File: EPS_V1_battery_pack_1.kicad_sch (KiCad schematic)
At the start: 29 parts, among them U1 MP2672AGD-0000-Z, U5 MAX17205G+

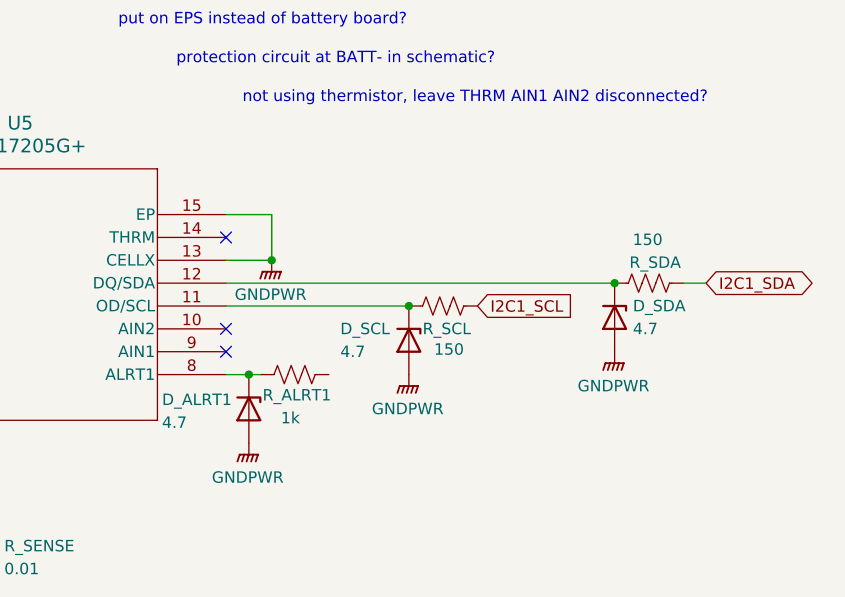
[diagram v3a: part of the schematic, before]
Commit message: Add fuel gauge ALRT lines
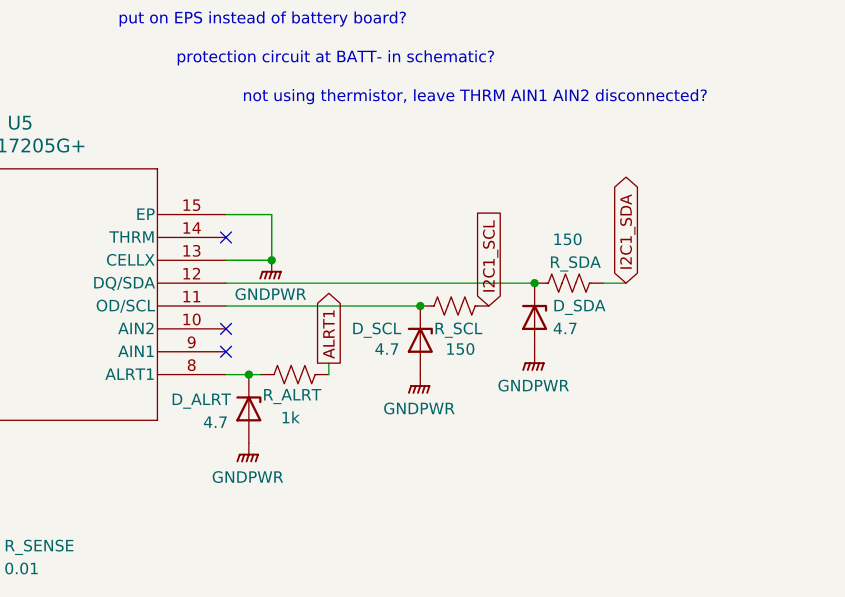
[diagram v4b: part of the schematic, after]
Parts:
- renumbered D_ALRT1 to D_ALRT, R_ALRT1 to R_ALRT
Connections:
- net ALRT1: now reaches R_ALRT.2
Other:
- moved on the sheet: D_SCL, D_SDA, R_SCL, R_SDA
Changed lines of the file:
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@@
 	)
 	(junction
-		(at 260.35 80.01)
+		(at 251.46 80.01)
 		(diameter 0)
 		(color 0 0 0 0)
@@
 	)
 	(junction
-		(at 237.49 82.55)
+		(at 238.76 82.55)
 		(diameter 0)
 		(color 0 0 0 0)
@@
 	(wire
 		(pts
+			(xy 228.6 88.9) (xy 228.6 90.17)
+		)
+		(stroke
+			(width 0)
+			(type default)
+		)
+	)
+	(wire
+		(pts
 			(xy 166.37 77.47) (xy 171.45 77.47)
 		)
@@
 	(wire
 		(pts
-			(xy 217.17 80.01) (xy 260.35 80.01)
+			(xy 217.17 80.01) (xy 251.46 80.01)
 		)
 		(stroke
@@
 	(wire
 		(pts
-			(xy 217.17 82.55) (xy 237.49 82.55)
+			(xy 217.17 82.55) (xy 238.76 82.55)
 		)
 		(stroke
@@
 	(wire
 		(pts
-			(xy 270.51 80.01) (xy 267.97 80.01)
+			(xy 261.62 80.01) (xy 259.08 80.01)
 		)
 		(stroke
@@
 		)
 	)
+	(global_label "ALRT1"
+		(shape output)
+		(at 228.6 88.9 90)
+		(fields_autoplaced yes)
+		(effects
+			(font
+				(size 1.27 1.27)
+			)
+			(justify left)
+		)
+		(property "Intersheetrefs" "${INTERSHEET_REFS}"
+			(at 228.6 80.351 90)
+			(effects
+				(font
+					(size 1.27 1.27)
+				)
+				(justify left)
+				(hide yes)
+			)
+		)
+	)
 	(global_label "I2C1_SDA"
 		(shape bidirectional)
-		(at 270.51 80.01 0)
+		(at 261.62 80.01 90)
 		(fields_autoplaced yes)
 		(effects
@@
 		)
 		(property "Intersheetrefs" "${INTERSHEET_REFS}"
-			(at 283.436 80.01 0)
+			(at 261.62 67.084 90)
 			(effects
 				(font
@@
 	(global_label "I2C1_SCL"
 		(shape input)
-		(at 245.11 82.55 0)
+		(at 246.38 82.55 90)
 		(fields_autoplaced yes)
 		(effects
@@
 		)
 		(property "Intersheetrefs" "${INTERSHEET_REFS}"
-			(at 256.8642 82.55 0)
+			(at 246.38 70.7958 90)
 			(effects
 				(font
@@
 	(symbol
 		(lib_id "Device:R_US")
-		(at 264.16 80.01 90)
+		(at 255.27 80.01 90)
 		(unit 1)
 		(exclude_from_sim no)
@@
 		(dnp no)
 		(property "Reference" "R_SDA"
-			(at 267.716 77.724 90)
+			(at 258.826 77.724 90)
 			(effects
 				(font
@@
 		)
 		(property "Value" "150"
-			(at 265.684 75.184 90)
+			(at 256.794 75.184 90)
 			(effects
 				(font
@@
 		)
 		(property "Footprint" ""
-			(at 264.414 78.994 90)
+			(at 255.524 78.994 90)
 			(effects
 				(font
@@
 		)
 		(property "Datasheet" "~"
-			(at 264.16 80.01 0)
+			(at 255.27 80.01 0)
 			(effects
 				(font
@@
 		)
 		(property "Description" "Resistor, US symbol"
-			(at 264.16 80.01 0)
+			(at 255.27 80.01 0)
 			(effects
 				(font
@@
 		(on_board yes)
 		(dnp no)
-		(property "Reference" "R_ALRT1"
+		(property "Reference" "R_ALRT"
 			(at 221.234 92.456 90)
 			(effects
@@
 			(project "EPS_V1"
 				(path "/85157432-5d03-48fa-ab40-27ed3d133f47/d6a7ca1d-fe68-467f-8233-74a5cf811189"
-					(reference "R_ALRT1")
+					(reference "R_ALRT")
 					(unit 1)
 				)
@@
 	(symbol
 		(lib_id "power:GNDPWR")
-		(at 237.49 90.17 0)
+		(at 238.76 90.17 0)
 		(unit 1)
 		(exclude_from_sim no)
@@
 		(fields_autoplaced yes)
 		(property "Reference" "#PWR043"
-			(at 237.49 95.25 0)
+			(at 238.76 95.25 0)
 			(effects
 				(font
@@
 		)
 		(property "Value" "GNDPWR"
-			(at 237.363 93.98 0)
+			(at 238.633 93.98 0)
 			(effects
 				(font
@@
 		)
 		(property "Footprint" ""
-			(at 237.49 91.44 0)
+			(at 238.76 91.44 0)
 			(effects
 				(font
@@
 		)
 		(property "Datasheet" ""
-			(at 237.49 91.44 0)
+			(at 238.76 91.44 0)
 			(effects
 				(font
@@
 		)
 		(property "Description" "Power symbol creates a global label with name \"GNDPWR\" , global ground"
-			(at 237.49 90.17 0)
+			(at 238.76 90.17 0)
 			(effects
 				(font
@@
 	(symbol
 		(lib_id "Device:D_Zener")
-		(at 260.35 83.82 270)
+		(at 251.46 83.82 270)
 		(unit 1)
 		(exclude_from_sim no)
@@
 		(dnp no)
 		(property "Reference" "D_SDA"
-			(at 262.382 82.55 90)
+			(at 253.492 82.55 90)
 			(effects
 				(font
@@
 		)
 		(property "Value" "4.7"
-			(at 262.382 85.09 90)
+			(at 253.492 85.09 90)
 			(effects
 				(font
@@
 		)
 		(property "Footprint" ""
-			(at 260.35 83.82 0)
+			(at 251.46 83.82 0)
 			(effects
 				(font
@@
 		)
 		(property "Datasheet" "~"
-			(at 260.35 83.82 0)
+			(at 251.46 83.82 0)
 			(effects
 				(font
@@
 		)
 		(property "Description" "Zener diode"
-			(at 260.35 83.82 0)
+			(at 251.46 83.82 0)
 			(effects
 				(font
@@
 	(symbol
 		(lib_id "Device:R_US")
-		(at 241.3 82.55 90)
+		(at 242.57 82.55 90)
 		(unit 1)
 		(exclude_from_sim no)
@@
 		(dnp no)
 		(property "Reference" "R_SCL"
-			(at 239.014 85.09 90)
+			(at 240.284 85.09 90)
 			(effects
 				(font
@@
 		)
 		(property "Value" "150"
-			(at 240.284 87.376 90)
+			(at 241.554 87.376 90)
 			(effects
 				(font
@@
 		)
 		(property "Footprint" ""
-			(at 241.554 81.534 90)
+			(at 242.824 81.534 90)
 			(effects
 				(font
@@
 		)
 		(property "Datasheet" "~"
-			(at 241.3 82.55 0)
+			(at 242.57 82.55 0)
 			(effects
 				(font
@@
 		)
 		(property "Description" "Resistor, US symbol"
-			(at 241.3 82.55 0)
+			(at 242.57 82.55 0)
 			(effects
 				(font
@@
 	(symbol
 		(lib_id "power:GNDPWR")
-		(at 260.35 87.63 0)
+		(at 251.46 87.63 0)
 		(unit 1)
 		(exclude_from_sim no)
@@
 		(fields_autoplaced yes)
 		(property "Reference" "#PWR044"
-			(at 260.35 92.71 0)
+			(at 251.46 92.71 0)
 			(effects
 				(font
@@
 		)
 		(property "Value" "GNDPWR"
-			(at 260.223 91.44 0)
+			(at 251.333 91.44 0)
 			(effects
 				(font
@@
 		)
 		(property "Footprint" ""
-			(at 260.35 88.9 0)
+			(at 251.46 88.9 0)
 			(effects
 				(font
@@
 		)
 		(property "Datasheet" ""
-			(at 260.35 88.9 0)
+			(at 251.46 88.9 0)
 			(effects
 				(font
@@
 		)
 		(property "Description" "Power symbol creates a global label with name \"GNDPWR\" , global ground"
-			(at 260.35 87.63 0)
+			(at 251.46 87.63 0)
 			(effects
 				(font
@@
 		(on_board yes)
 		(dnp no)
-		(property "Reference" "D_ALRT1"
-			(at 210.058 92.964 90)
+		(property "Reference" "D_ALRT"
+			(at 211.074 92.964 90)
 			(effects
 				(font
@@
 		)
 		(property "Value" "4.7"
-			(at 210.058 95.504 90)
+			(at 214.63 95.504 90)
 			(effects
 				(font
@@
 			(project ""
 				(path "/85157432-5d03-48fa-ab40-27ed3d133f47/d6a7ca1d-fe68-467f-8233-74a5cf811189"
-					(reference "D_ALRT1")
+					(reference "D_ALRT")
 					(unit 1)
 				)
@@
 	(symbol
 		(lib_id "Device:D_Zener")
-		(at 237.49 86.36 270)
+		(at 238.76 86.36 270)
 		(unit 1)
 		(exclude_from_sim no)
@@
 		(dnp no)
 		(property "Reference" "D_SCL"
-			(at 229.87 85.09 90)
+			(at 231.14 85.09 90)
 			(effects
 				(font
@@
 		)
 		(property "Value" "4.7"
-			(at 229.87 87.63 90)
+			(at 233.68 87.376 90)
 			(effects
 				(font
@@
 		)
 		(property "Footprint" ""
-			(at 237.49 86.36 0)
+			(at 238.76 86.36 0)
 			(effects
 				(font
@@
 		)
 		(property "Datasheet" "~"
-			(at 237.49 86.36 0)
+			(at 238.76 86.36 0)
 			(effects
 				(font
@@
 		)
 		(property "Description" "Zener diode"
-			(at 237.49 86.36 0)
+			(at 238.76 86.36 0)
 			(effects
 				(font

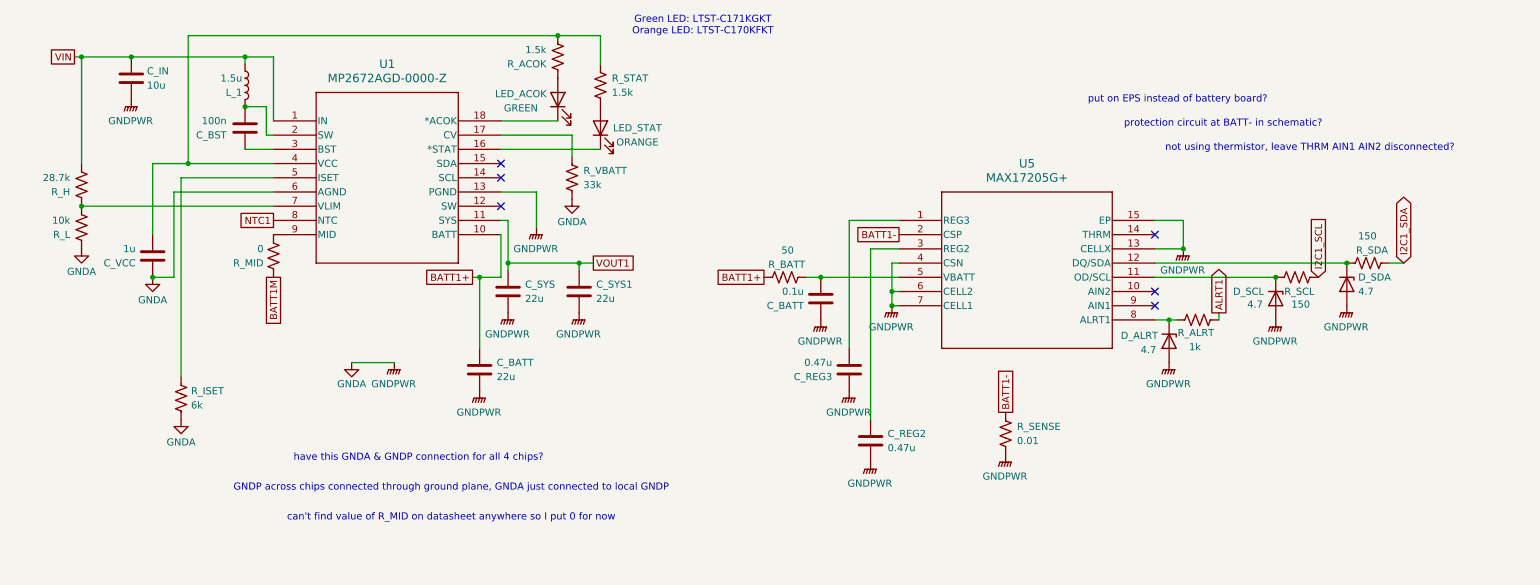
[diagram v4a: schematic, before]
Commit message: Add boost converter to 12V, fix grounding
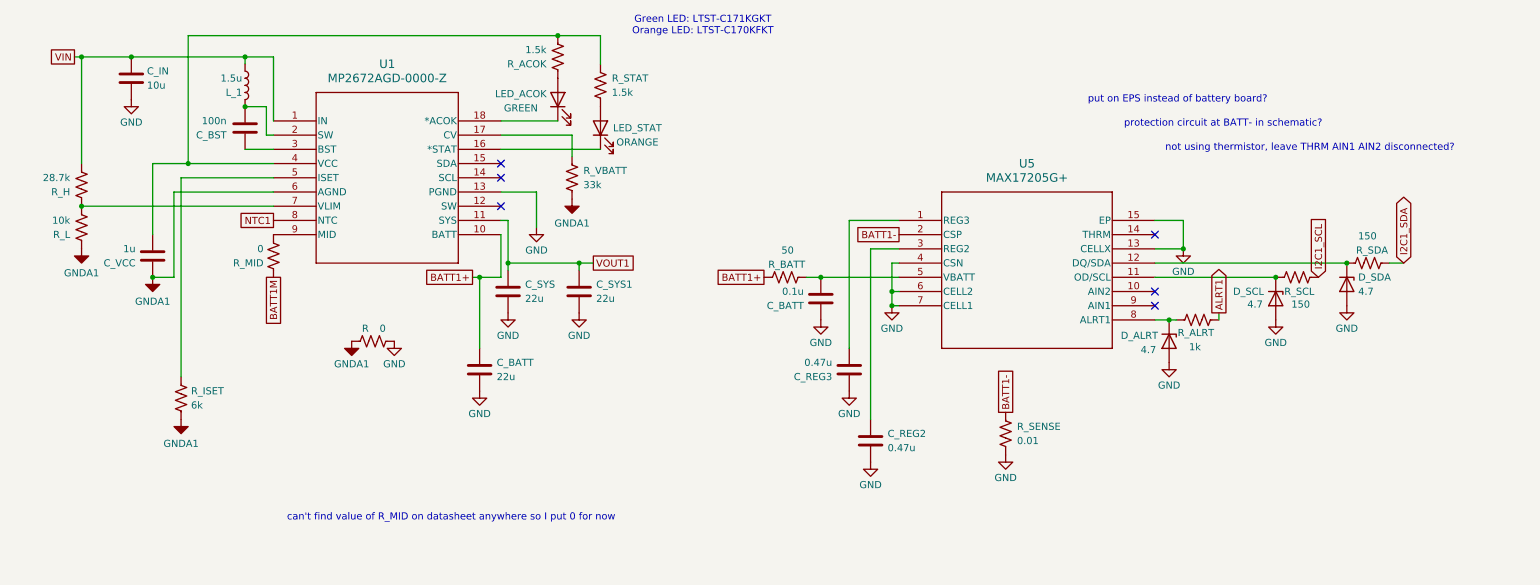
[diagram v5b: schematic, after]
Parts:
- added R: 0, symbol Device:R_US
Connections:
- net GNDA renamed GND
- net GND: now also R.2; no longer C_VCC.1, R_ISET.2, R_L.1, R_VBATT.2, U1.6 (AGND)
- new net GNDA1: C_VCC.1, R.1, R_ISET.2, R_L.1, R_VBATT.2, U1.6 (AGND)
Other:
- note removed: "GNDP across chips connected through ground plane, GNDA just connected to local GNDP"
- note removed: "have this GNDA & GNDP connection for all 4 chips?"

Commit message: Add 12V boost values
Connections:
- net GND: no longer R_SENSE.2
- new net BATT_GND: R_SENSE.2
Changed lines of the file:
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@@
+		)
+	)
+	(global_label "BATT_GND"
+		(shape passive)
+		(at 190.5 114.3 270)
+		(fields_autoplaced yes)
+		(effects
+			(font
+				(size 1.27 1.27)
+			)
+			(justify right)
+		)
+		(property "Intersheetrefs" "${INTERSHEET_REFS}"
+			(at 190.5 125.3058 90)
+			(effects
+				(font
+					(size 1.27 1.27)
+				)
+				(justify right)
+				(hide yes)
+			)
 		)
 	)
@@
 					(unit 1)
 				)
-			)
-		)
-	)
-	(symbol
-		(lib_id "power:GND")
-		(at 190.5 114.3 0)
-		(unit 1)
-		(exclude_from_sim no)
-		(in_bom yes)
-		(on_board yes)
-		(dnp no)
-		(property "Reference" "#PWR03"
-			(at 190.5 120.65 0)
-			(effects
-				(font
-					(size 1.27 1.27)
-				)
-				(hide yes)
-			)
-		)
-		(property "Value" "GND"
-			(at 190.5 118.364 0)
-			(effects
-				(font
-					(size 1.27 1.27)
-				)
-			)
-		)
-		(property "Footprint" ""
-			(at 190.5 114.3 0)
-			(effects
-				(font
-					(size 1.27 1.27)
-				)
-				(hide yes)
-			)
-		)
-		(property "Datasheet" ""
-			(at 190.5 114.3 0)
-			(effects
-				(font
-					(size 1.27 1.27)
-				)
-				(hide yes)
-			)
-		)
-		(property "Description" "Power symbol creates a global label with name \"GND\" , ground"
-			(at 190.5 114.3 0)
-			(effects
-				(font
-					(size 1.27 1.27)
-				)
-				(hide yes)
-			)
-		)
-		(pin "1"
-		)
-		(instances
-			(project "EPS_V1"
-				(path "/85157432-5d03-48fa-ab40-27ed3d133f47/d6a7ca1d-fe68-467f-8233-74a5cf811189"
-					(reference "#PWR03")
-					(unit 1)
-				)

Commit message: Clarify global net naming, other minor fixes
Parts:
- added R7: 0, symbol Device:R_US
- R_MID: value 0 -> 50
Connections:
- net BATT_GND: now also R7.1; no longer R_SENSE.2
- net GND: no longer U5.15 (EP), U5.4 (CSN)
- net VIN renamed CHG_IN
- net VOUT1 renamed CHG_OUT1
- new net: R7.2, R_SENSE.2, U5.15 (EP), U5.4 (CSN)
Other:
- note added: "50 ohm R_MID value from fuel gauge datasheet"
- note removed: "protection circuit at BATT- in schematic?"
- note removed: "put on EPS instead of battery board?"
- moved on the sheet: R_SENSE

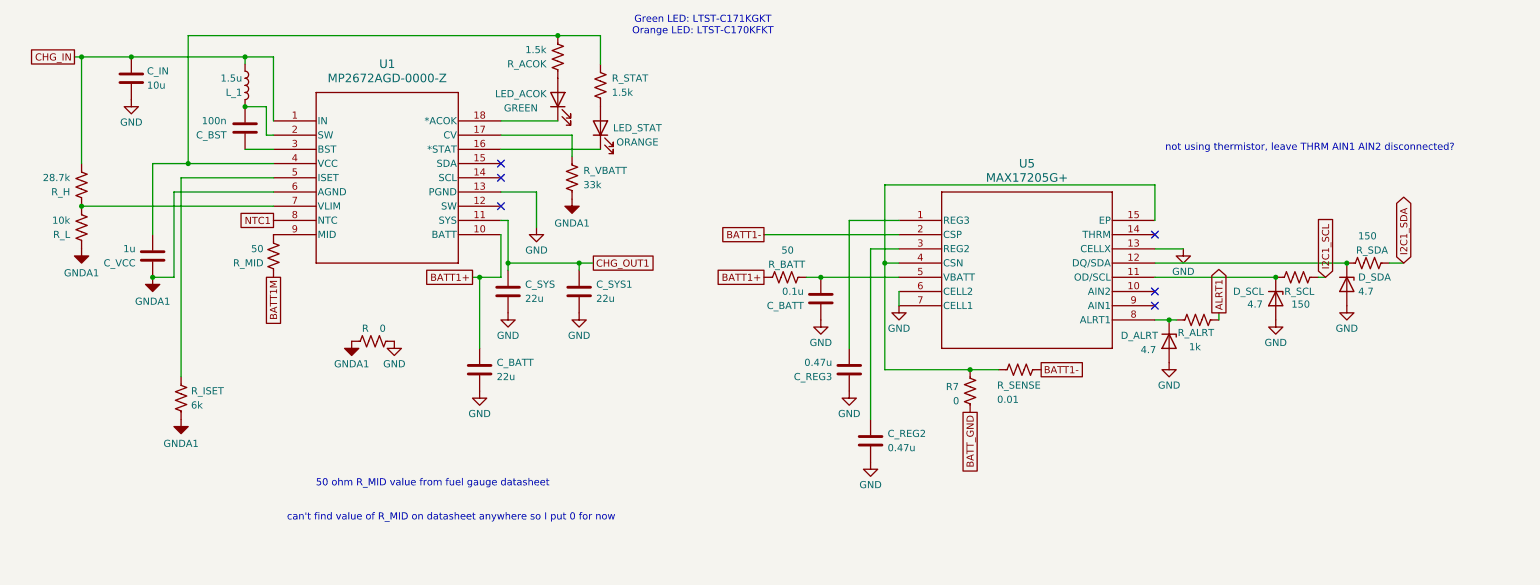
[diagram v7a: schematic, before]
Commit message: Add all footprints except connectors & switches, change to net ties over 0 ohm resistors
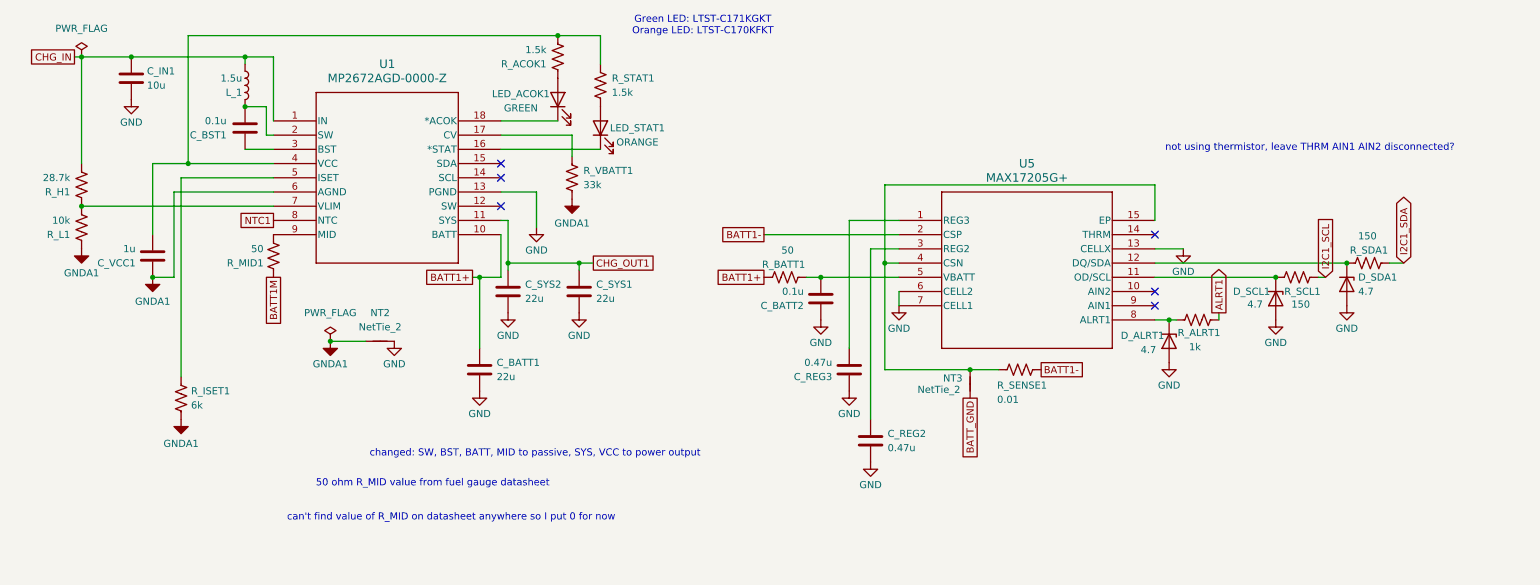
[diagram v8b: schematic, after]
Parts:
- removed R, R7: 0, symbol Device:R_US
- added NT2, NT3: NetTie_2, NetTie:NetTie-2_SMD_Pad2.0mm, symbol Device:NetTie_2
- C_BATT1: renamed from C_BATT; footprint (none) -> Capacitor_SMD:C_0805_2012Metric; Voltage Rating (none) -> 25V
- C_BATT2: renamed from C_BATT; footprint (none) -> Capacitor_SMD:C_0603_1608Metric; Voltage Rating (none) -> 16V
- C_BST1: renamed from C_BST; value 100n -> 0.1u; footprint (none) -> Capacitor_SMD:C_0603_1608Metric; Voltage Rating (none) -> 16V
- C_IN1: renamed from C_IN; footprint (none) -> Capacitor_SMD:C_0805_2012Metric; Voltage Rating (none) -> 25V
- C_REG2, C_REG3: footprint (none) -> Capacitor_SMD:C_0603_1608Metric; Voltage Rating (none) -> 16V
- C_SYS1: footprint (none) -> Capacitor_SMD:C_0805_2012Metric; Voltage Rating (none) -> 25V
- C_SYS2: renamed from C_SYS; footprint (none) -> Capacitor_SMD:C_0805_2012Metric; Voltage Rating (none) -> 25V
- C_VCC1: renamed from C_VCC; footprint (none) -> Capacitor_SMD:C_0603_1608Metric; Voltage Rating (none) -> 16V
- D_ALRT1: renamed from D_ALRT; footprint (none) -> Diode_SMD:D_0603_1608Metric; MPN (none) -> TVSL02V05C005 (check)
- D_SCL1: renamed from D_SCL; footprint (none) -> Diode_SMD:D_0603_1608Metric; MPN (none) -> TVSL02V05C005 (check)
- D_SDA1: renamed from D_SDA; footprint (none) -> Diode_SMD:D_0603_1608Metric; MPN (none) -> TVSL02V05C005 (check)
- LED_ACOK1: renamed from LED_ACOK; footprint (none) -> LED_SMD:LED_0805_2012Metric; MPN (none) -> LTST-C171KGKT
- LED_STAT1: renamed from LED_STAT; footprint (none) -> LED_SMD:LED_0805_2012Metric; MPN (none) -> LTST-C170KFKT
- L_1: footprint (none) -> AMELA2012S_1R5MT:IND_AMELA2012S-1R5MT; MPN (none) -> AMELA2012S-1R5MT
- R_ACOK1: renamed from R_ACOK; footprint (none) -> Resistor_SMD:R_0603_1608Metric
- R_ALRT1: renamed from R_ALRT; footprint (none) -> Resistor_SMD:R_0603_1608Metric
- R_BATT1: renamed from R_BATT; footprint (none) -> Resistor_SMD:R_0603_1608Metric
- R_H1: renamed from R_H; footprint (none) -> Resistor_SMD:R_0603_1608Metric
- R_ISET1: renamed from R_ISET; footprint (none) -> Resistor_SMD:R_0603_1608Metric
- R_L1: renamed from R_L; footprint (none) -> Resistor_SMD:R_0603_1608Metric
- R_MID1: renamed from R_MID; footprint (none) -> Resistor_SMD:R_0603_1608Metric
- R_SCL1: renamed from R_SCL; footprint (none) -> Resistor_SMD:R_0603_1608Metric
- R_SDA1: renamed from R_SDA; footprint (none) -> Resistor_SMD:R_0603_1608Metric
- R_SENSE1: renamed from R_SENSE; footprint (none) -> Resistor_SMD:R_0603_1608Metric
- R_STAT1: renamed from R_STAT; footprint (none) -> Resistor_SMD:R_0603_1608Metric
- R_VBATT1: renamed from R_VBATT; footprint (none) -> Resistor_SMD:R_0603_1608Metric
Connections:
- net BATT_GND: now also NT3.1
- net GND: now also NT2.2
- net GNDA1: now also NT2.1
- net at R_SENSE1.2, U5.15 (EP), U5.4 (CSN): now also NT3.2
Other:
- note added: "changed: SW, BST, BATT, MID to passive, SYS, VCC to power output"
